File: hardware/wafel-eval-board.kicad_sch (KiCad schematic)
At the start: 53 parts, among them J101 CAN PORT, J102 SW, Q101 AO3422, U101 LM5163DDA

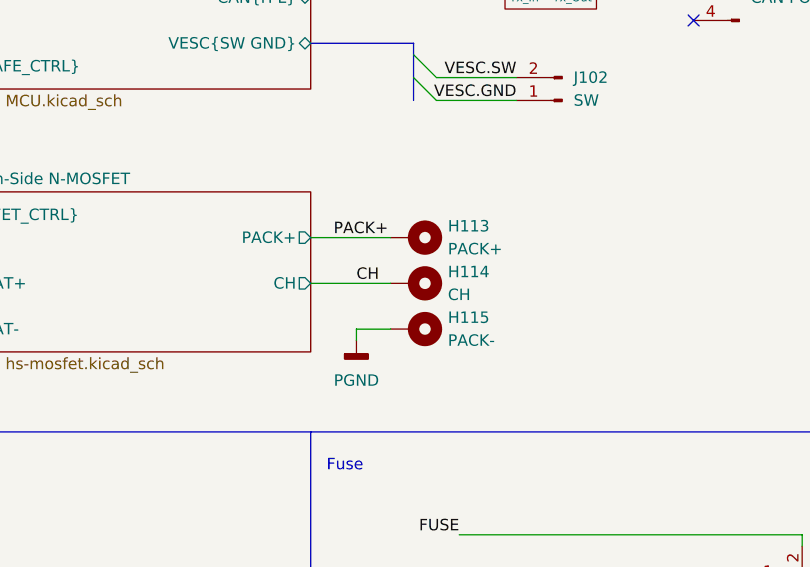
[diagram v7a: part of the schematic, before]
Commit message: added qulon zone
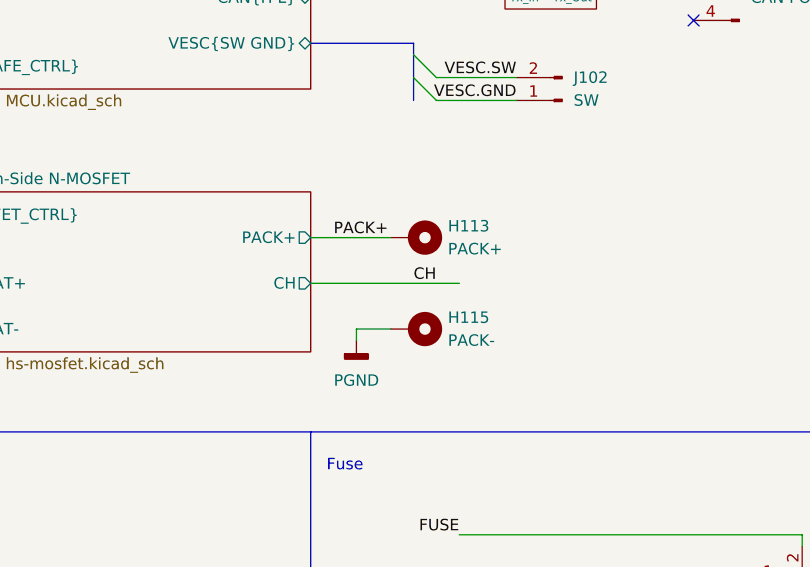
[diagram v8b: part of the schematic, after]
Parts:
- removed H114: CH, MountingHole:MountingHole_3.2mm_M3_Pad, symbol Mechanical:MountingHole_Pad
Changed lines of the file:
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@@
 	(wire
 		(pts
-			(xy 187.96 92.71) (xy 196.85 92.71)
+			(xy 187.96 92.71) (xy 204.47 92.71)
 		)
 		(stroke
@@
 	)
 	(label "CH"
-		(at 193.04 92.71 0)
+		(at 199.39 92.71 0)
 		(effects
 			(font
@@
 					(unit 1)
 				)
-			)
-		)
-	)
-	(symbol
-		(lib_id "Mechanical:MountingHole_Pad")
-		(at 199.39 92.71 270)
-		(mirror x)
-		(unit 1)
-		(body_style 1)
-		(exclude_from_sim no)
-		(in_bom no)
-		(on_board yes)
-		(in_pos_files yes)
-		(dnp no)
-		(property "Reference" "H114"
-			(at 203.2 91.4399 90)
-			(show_name no)
-			(do_not_autoplace no)
-			(effects
-				(font
-					(size 1.27 1.27)
-				)
-				(justify left)
-			)
-		)
-		(property "Value" "CH"
-			(at 203.2 93.9799 90)
-			(show_name no)
-			(do_not_autoplace no)
-			(effects
-				(font
-					(size 1.27 1.27)
-				)
-				(justify left)
-			)
-		)
-		(property "Footprint" "MountingHole:MountingHole_3.2mm_M3_Pad"
-			(at 199.39 92.71 0)
-			(hide yes)
-			(show_name no)
-			(do_not_autoplace no)
-			(effects
-				(font
-					(size 1.27 1.27)
-				)
-			)
-		)
-		(property "Datasheet" ""
-			(at 199.39 92.71 0)
-			(hide yes)
-			(show_name no)
-			(do_not_autoplace no)
-			(effects
-				(font
-					(size 1.27 1.27)
-				)
-			)
-		)
-		(property "Description" "Mounting Hole with connection"
-			(at 199.39 92.71 0)
-			(hide yes)
-			(show_name no)
-			(do_not_autoplace no)
-			(effects
-				(font
-					(size 1.27 1.27)
-				)
-			)
-		)
-		(pin "1"
-		)
-		(instances
-			(project "wafel-eval-board"
-				(path "/3e668e3e-3e16-4665-a807-4735962c41d3"
-					(reference "H114")
-					(unit 1)
-				)
